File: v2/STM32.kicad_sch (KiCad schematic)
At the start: 53 parts, among them J1 USB_B_Micro, J2 Conn_ARM_JTAG_SWD_10, SW1 SW_Push, SW2 SW_Push, U1 STM32H723VETx, U5 TPD4E05U06DQA, U6 TPD4E05U06DQA, U8 SN74LXC1T14DCKR, Y1 8 MHz

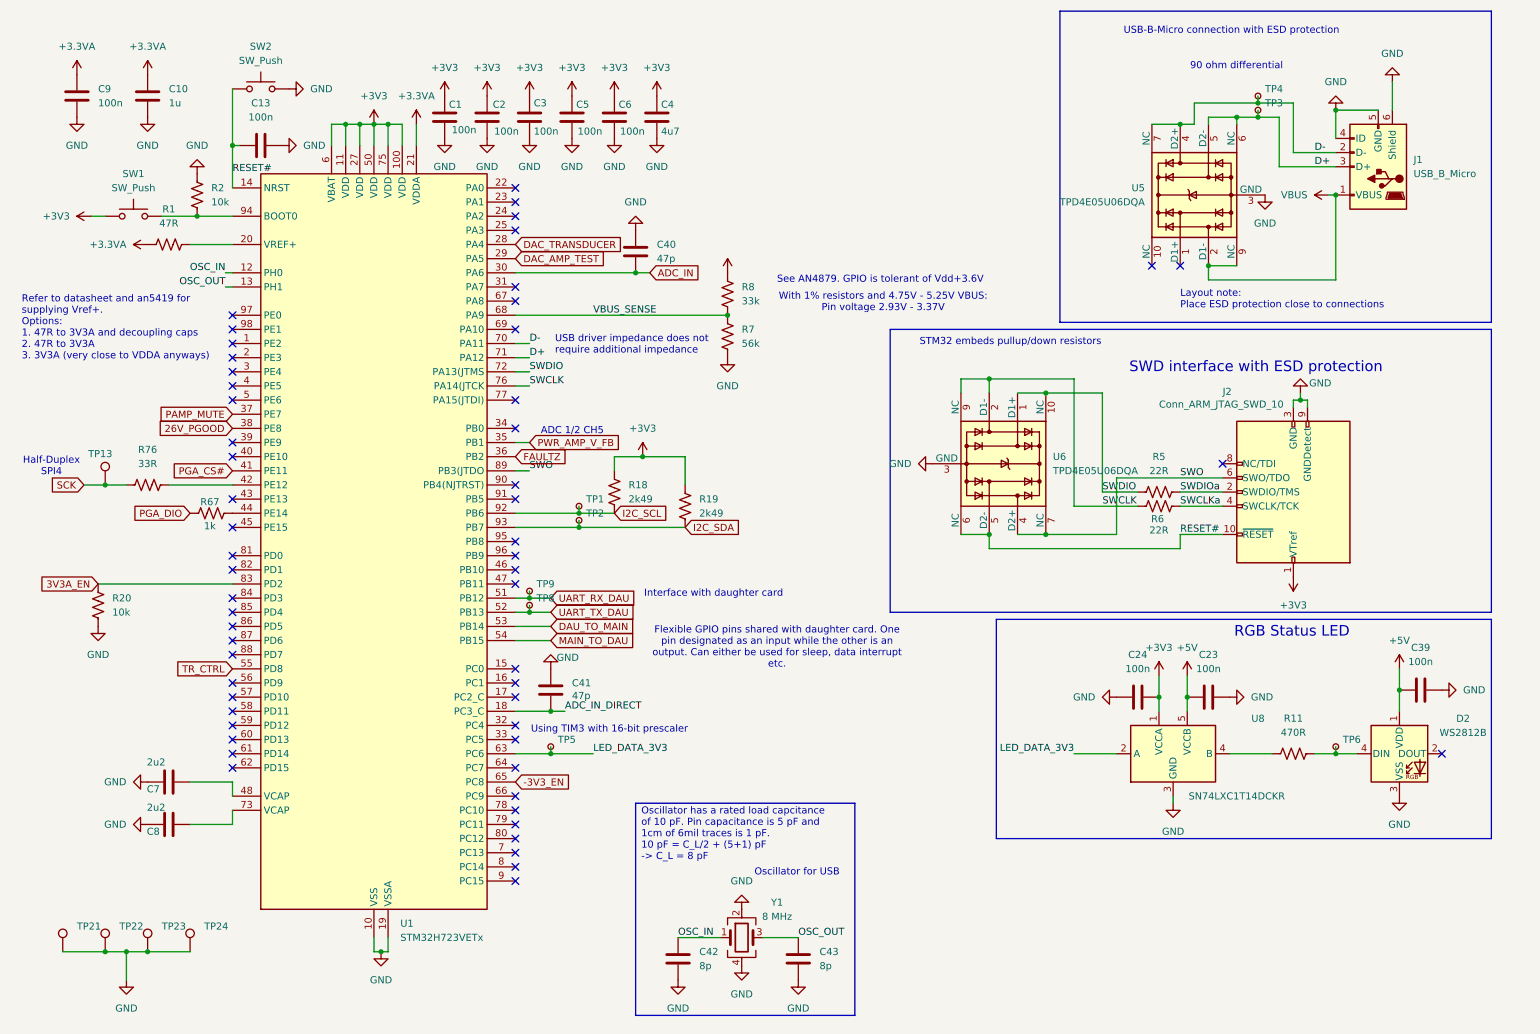
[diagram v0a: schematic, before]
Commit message: Most v2 changes made
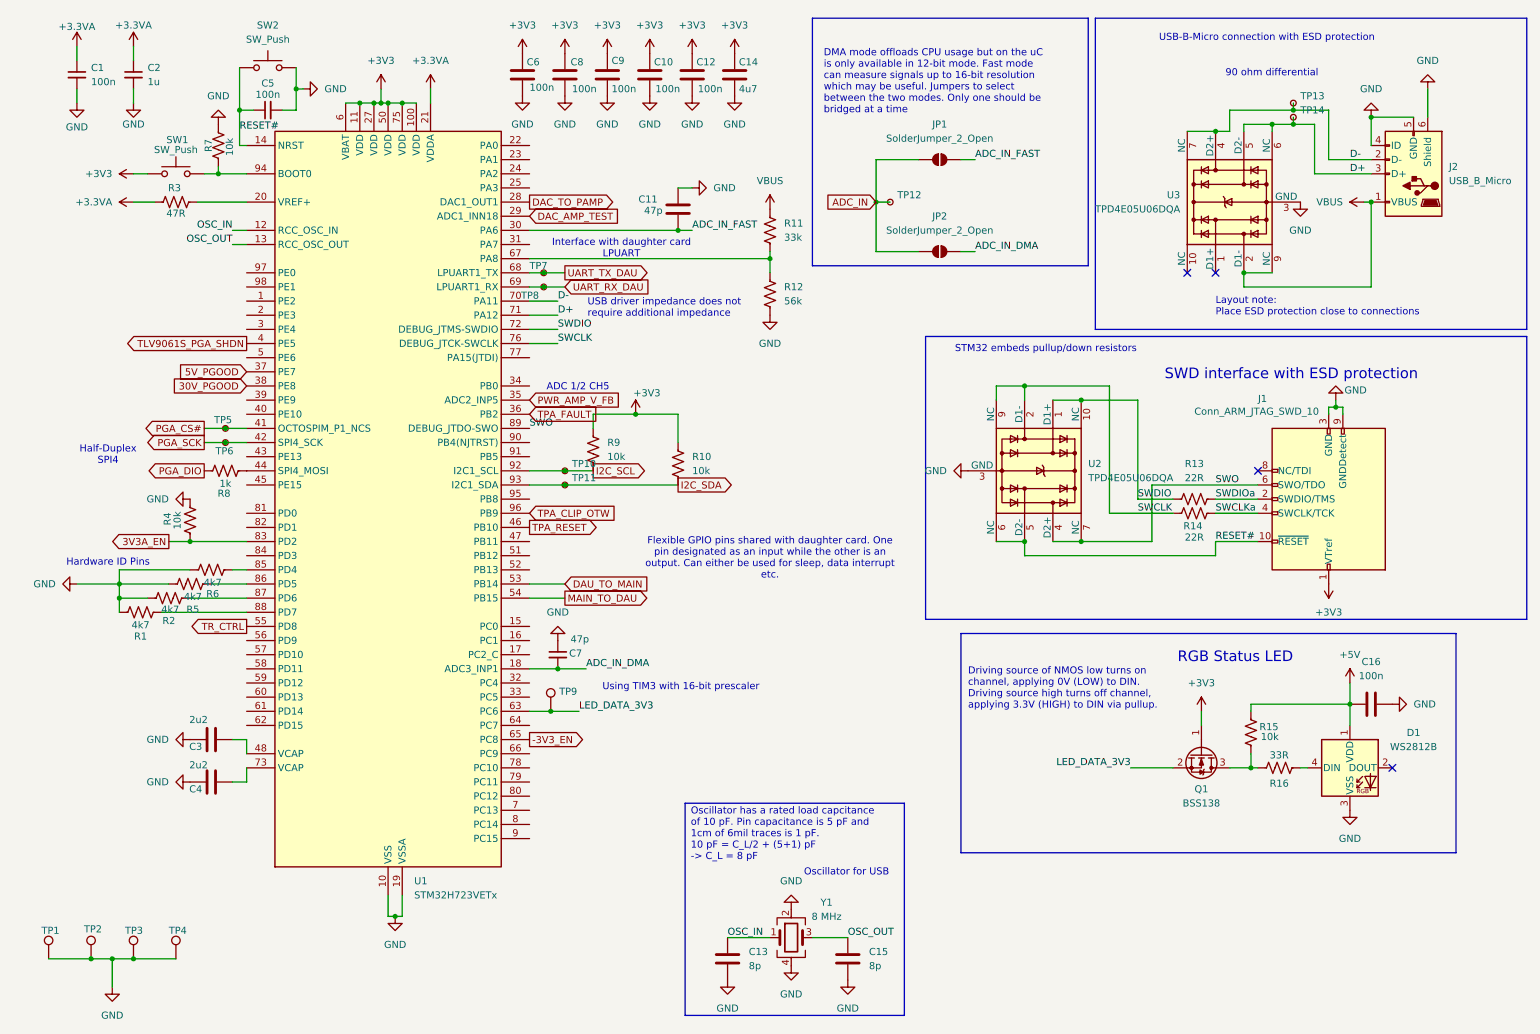
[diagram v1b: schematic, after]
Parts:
- removed C1, C2, C23, C24, C39, C5: 100n, Capacitor_SMD:C_0603_1608Metric_Pad1.08x0.95mm_HandSolder, symbol UAM_symbols:C
- removed C40, C41: 47p, Capacitor_SMD:C_0603_1608Metric_Pad1.08x0.95mm_HandSolder, symbol UAM_symbols:C
- removed C42, C43: 8p, Capacitor_SMD:C_0603_1608Metric_Pad1.08x0.95mm_HandSolder, symbol UAM_symbols:C
- removed C7: 2u2, Capacitor_SMD:C_0603_1608Metric_Pad1.08x0.95mm_HandSolder, symbol UAM_symbols:C
- removed D2: WS2812B, LED_SMD:LED_WS2812B_PLCC4_5.0x5.0mm_P3.2mm, symbol UAM_symbols:WS2812B
- removed J1: USB_B_Micro, Connector_USB:USB_Micro-B_Amphenol_10118193-0001LF_Horizontal, symbol UAM_symbols:USB_B_Micro
- removed J2: Conn_ARM_JTAG_SWD_10, Connector_PinHeader_1.27mm:PinHeader_2x05_P1.27mm_Vertical, symbol UAM_symbols:Conn_ARM_JTAG_SWD_10
- removed R1: 47R, Resistor_SMD:R_0603_1608Metric_Pad0.98x0.95mm_HandSolder, symbol UAM_symbols:R_US
- removed R11: 470R, Resistor_SMD:R_0603_1608Metric_Pad0.98x0.95mm_HandSolder, symbol UAM_symbols:R_US
- removed R18, R19: 2k49, Resistor_SMD:R_0603_1608Metric_Pad0.98x0.95mm_HandSolder, symbol UAM_symbols:R_US
- removed R2, R20: 10k, Resistor_SMD:R_0603_1608Metric_Pad0.98x0.95mm_HandSolder, symbol UAM_symbols:R_US
- removed R5, R6: 22R, Resistor_SMD:R_0603_1608Metric_Pad0.98x0.95mm_HandSolder, symbol UAM_symbols:R_US
- removed R67: 1k, Resistor_SMD:R_0603_1608Metric_Pad0.98x0.95mm_HandSolder, symbol UAM_symbols:R_US
- removed R7: 56k, Resistor_SMD:R_0603_1608Metric_Pad0.98x0.95mm_HandSolder, symbol UAM_symbols:R_US
- removed R76: 33R, Resistor_SMD:R_0603_1608Metric_Pad0.98x0.95mm_HandSolder, symbol UAM_symbols:R_US
- removed R8: 33k, Resistor_SMD:R_0603_1608Metric_Pad0.98x0.95mm_HandSolder, symbol UAM_symbols:R_US
- removed SW1, SW2: SW_Push, Switches:EVP-AWED4A (3.00mm x 2.00mm), symbol UAM_symbols:SW_Push
- removed TP1, TP2, TP3, TP4, TP9: TestPoint_Small, TestPoint:TestPoint_Pad_D1.0mm, symbol UAM_symbols:TestPoint_Small
- removed TP13: TestPoint, TestPoint:TestPoint_Pad_D1.0mm, symbol UAM_symbols:TestPoint
- removed U5, U6: TPD4E05U06DQA, Package_SON:USON-10_2.5x1.0mm_P0.5mm, symbol UAM_symbols:TPD4E05U06DQA
- removed U8: SN74LXC1T14DCKR, Package_TO_SOT_SMD:SOT-353_SC-70-5, symbol UAM_symbols:SN74AUP1T34DCK
- added C1, C5: 100n, symbol Device:C_Small
- added C11: 47p, symbol Device:C
- added C12, C16: 100n, Capacitor_SMD:C_0603_1608Metric_Pad1.08x0.95mm_HandSolder, symbol UAM_symbols:C
- added C14: 4u7, Capacitor_SMD:C_0603_1608Metric_Pad1.08x0.95mm_HandSolder, symbol UAM_symbols:C
- added C15: 8p, Capacitor_SMD:C_0603_1608Metric_Pad1.08x0.95mm_HandSolder, symbol UAM_symbols:C
- added C2: 1u, symbol Device:C_Small
- added C7: 47p, symbol Device:C_Small
- added D1: WS2812B, LED_SMD:LED_WS2812B_PLCC4_5.0x5.0mm_P3.2mm, symbol UAM_symbols:WS2812B
- added J1: Conn_ARM_JTAG_SWD_10, Connector_PinHeader_1.27mm:PinHeader_2x05_P1.27mm_Vertical, symbol UAM_symbols:Conn_ARM_JTAG_SWD_10
- added J2: USB_B_Micro, Connector_USB:USB_Micro-B_Amphenol_10118193-0001LF_Horizontal, symbol UAM_symbols:USB_B_Micro
- added JP1, JP2: SolderJumper_2_Open, Jumper:SolderJumper-2_P1.3mm_Open_RoundedPad1.0x1.5mm, symbol UAM_symbols:SolderJumper_2_Open
- added Q1: BSS138, Package_TO_SOT_SMD:SOT-23, symbol UAM_symbols:BSS138
- added R1, R2, R5, R6: 4k7, symbol Device:R_US
- added R10, R15, R4, R7, R9: 10k, symbol Device:R_US
- added R11: 33k, symbol Device:R_US
- added R12: 56k, symbol Device:R_US
- added R13, R14: 22R, Resistor_SMD:R_0603_1608Metric_Pad0.98x0.95mm_HandSolder, symbol UAM_symbols:R_US
- added R16: 33R, symbol Device:R_US
- added R3: 47R, symbol Device:R_US
- added R8: 1k, symbol Device:R_US
- added SW1, SW2: SW_Push, symbol Switch:SW_Push
- added TP10, TP11, TP7: TestPoint_Small, symbol UAM_symbols:TestPoint_Small
- added TP12, TP13, TP14: TestPoint_Small, TestPoint:TestPoint_Pad_D1.0mm, symbol UAM_symbols:TestPoint_Small
- added TP9: TestPoint, symbol UAM_symbols:TestPoint
- added U2, U3: TPD4E05U06DQA, Package_SON:USON-10_2.5x1.0mm_P0.5mm, symbol UAM_symbols:TPD4E05U06DQA
- C10: value 1u -> 100n
- C13: value 100n -> 8p
- C3: value 100n -> 2u2; ESR (none) -> <100
- C4: value 4u7 -> 2u2; ESR (none) -> < 100
- C8: value 2u2 -> 100n; ESR < 100 -> (none)
- TP5, TP6, TP8: footprint TestPoint:TestPoint_Pad_D1.0mm -> (none)
- renumbered TP21 to TP1, TP22 to TP2, TP23 to TP3, TP24 to TP4
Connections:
- net VBUS_SENSE is gone; now on net UART_TX_DAU: U1.68 (PA9)
- net +3.3VA: now also C1.1, C2.1, R3.1; no longer C10.1, C9.1
- net +3V3: now also C10.1, C8.1, C9.1, C12.1, C14.1, J1.1 (VTref), Q1.1 (G), R10.1, R9.1, SW1.1; no longer C3.1, C4.1
- net +5V: now also C16.1, D1.1 (VDD), R15.1
- net 3V3A_EN: now also R4.2
- net ADC_IN: now also JP1.1 (A), JP2.1 (A), TP12.1; no longer U1.30 (PA6)
- net D+: now also J2.3 (D+), TP14.1, U3.5 (D2-), U3.6 (NC)
- net D-: now also J2.2 (D-), TP13.1, U3.4 (D2+), U3.7 (NC)
- net GND: now also C3.1, C4.1, C8.2, C1.2, C11.1, C12.2, C14.2, C15.2, C16.2, C2.2, C5.2, C7.1, D1.3 (VSS), J1.3 (GND), J1.5 (GND), J1.9 (GNDDetect), J2.4 (ID), J2.5 (GND), J2.6 (Shield), R1.1, R12.2, R2.1, R4.1, R5.1, R6.1, R7.2, SW2.2, U2.3 (GND), U2.8 (GND), U3.3 (GND), U3.8 (GND); no longer C3.2, C4.2, C8.1
- net I2C_SCL: now also R9.2, TP10.1
- net I2C_SDA: now also R10.2, TP11.1
- net LED_DATA_3V3: now also Q1.2 (S), TP9.1; no longer TP5.1
- net OSC_IN: now also C13.1
- net OSC_OUT: now also C15.1
- net PGA_CS#: now also TP5.1
- net PGA_DIO: now also R8.1
- net RESET#: now also C5.1, J1.10 (~{RESET}), SW2.1, U2.5 (D2-), U2.6 (NC); no longer C13.1
- net SWCLK: now also R14.1, U2.2 (D1-), U2.9 (NC)
- net SWCLKa: now also J1.4 (SWCLK/TCK), R14.2
- net SWDIO: now also R13.1, U2.1 (D1+), U2.10 (NC)
- net SWDIOa: now also J1.2 (SWDIO/TMS), R13.2
- net SWO: now also J1.6 (SWO/TDO), U2.4 (D2+), U2.7 (NC)
- net UART_RX_DAU: now also TP8.1, U1.69 (PA10); no longer U1.51 (PB12)
- net UART_TX_DAU: now also TP7.1; no longer TP8.1, U1.52 (PB13)
- net VBUS: now also J2.1 (VBUS), R11.1, U3.2 (D1-), U3.9 (NC)
- net at U1.94 (BOOT0): now also R7.1, SW1.2
- net at U1.20 (VREF+): now also R3.2
- net PGA_SCK: now reaches TP6.1
- net PGA_SCK: now also U1.42 (PE12)
- net TLV9061S_PGA_SHDN: now reaches U1.4 (PE5)
- net at U1.44 (PE14): now also R8.2
- net TPA_RESET: now reaches U1.46 (PB10)
- net at U1.48 (VCAP): now also C3.2
- net at U1.67 (PA8): now also R11.2, R12.1
- net at U1.73 (VCAP): now also C4.2; no longer C8.2
- net at U1.85 (PD4): now also R6.2
- net at U1.86 (PD5): now also R5.2
- net at U1.87 (PD6): now also R2.2
- net at U1.88 (PD7): now also R1.2
- net TPA_CLIP_OTW: now reaches U1.96 (PB9)
- net 26V_PGOOD renamed 30V_PGOOD
- net ADC_IN_DIRECT renamed ADC_IN_DMA
- net ADC_IN_DMA: now also C7.2, JP2.2 (B)
- net DAC_TRANSDUCER renamed DAC_TO_PAMP
- net FAULTZ renamed TPA_FAULT
- net PAMP_MUTE renamed 5V_PGOOD
- new net: D1.4 (DIN), R16.2
- new net: Q1.3 (D), R15.2, R16.1
- new net ADC_IN_FAST: C11.2, JP1.2 (B), U1.30 (PA6)
- no-connect marks 57 -> 4
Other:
- note added: "DMA mode offloads CPU usage but on the uC is only available in 12-bit mode. Fast mode can measure signals up to 16-bit resolution which may be useful. Jumpers to select between the two modes. Only one should be bridged at a time"
- note added: "Driving source of NMOS low turns on channel, applying 0V (LOW) to DIN. Driving source high turns off channel, applying 3.3V (HIGH) to DIN via pullup."
- note added: "Hardware ID Pins"
- note added: "Interface with daughter card LPUART"
- note removed: "Interface with daughter card"
- note removed: "Refer to datasheet and an5419 for supplying Vref+. Options: 1. 47R to 3V3A and decoupling caps 2. 47R to 3V3A 3. 3V3A (very close to VDDA anyways)"
- note removed: "See AN4879. GPIO is tolerant of Vdd+3.6V"
- note removed: "With 1% resistors and 4.75V - 5.25V VBUS: Pin voltage 2.93V - 3.37V"
- moved on the sheet: TP1, TP2, TP3, TP4, Y1
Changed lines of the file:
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@@
 (kicad_sch
-	(version 20231120)
+	(version 20250114)
 	(generator "eeschema")
-	(generator_version "8.0")
+	(generator_version "9.0")
 	(paper "A4")
 	(title_block
